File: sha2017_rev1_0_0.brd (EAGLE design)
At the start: 95 x 86 mm, 205 parts, among them IC1 CP210X_USB_UART, IC2 AP7215, IC3 ESP32WROOM32, IC4 TP4056, IC5 FXL6408, IC6 CPT112, M1 MOTOR10MM, Q1 MMBT2222A, Q2 MMBT2222A, Q3 MMBT2222A, Q4 MMBT2222A, Q5 SI1304 BDL, Q6 MMBT2222A, X2 2908-05WB-MG, X4 JST-PH3

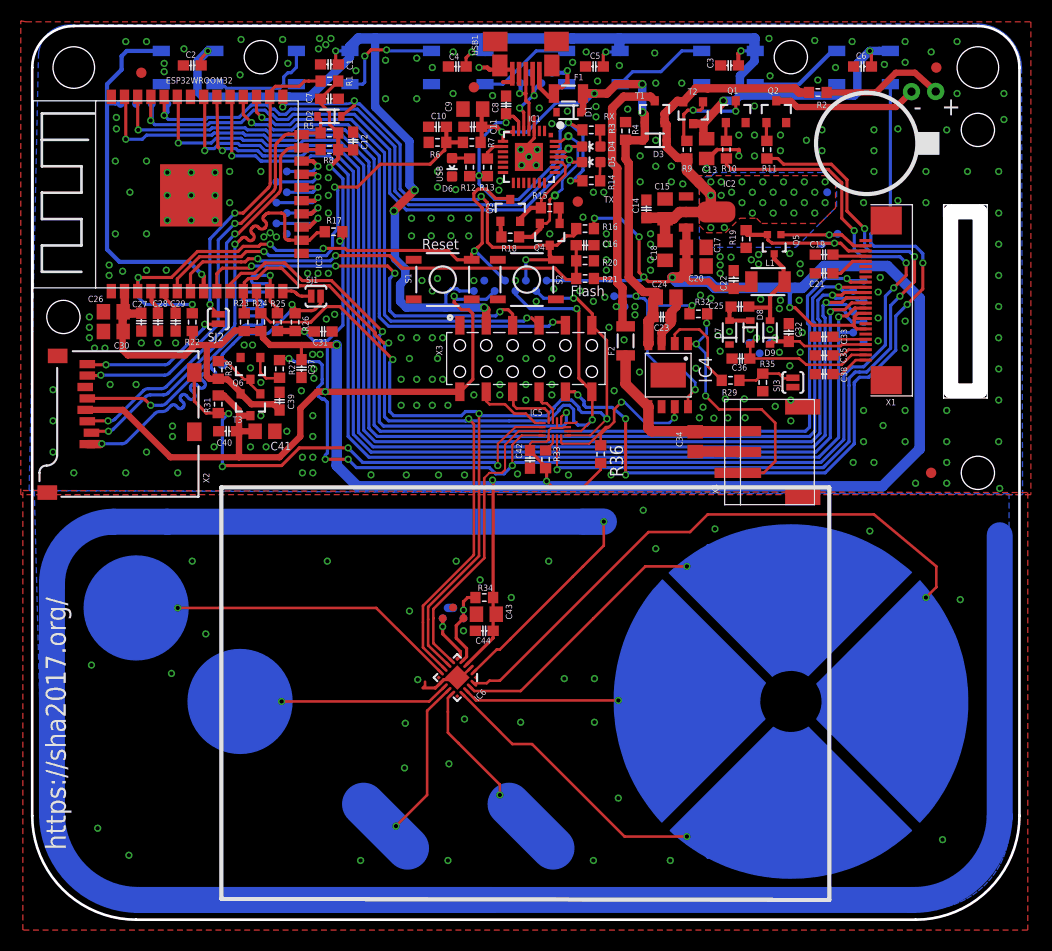
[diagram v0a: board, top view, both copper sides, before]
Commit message: Swap port expander and CPT112S for MPR121
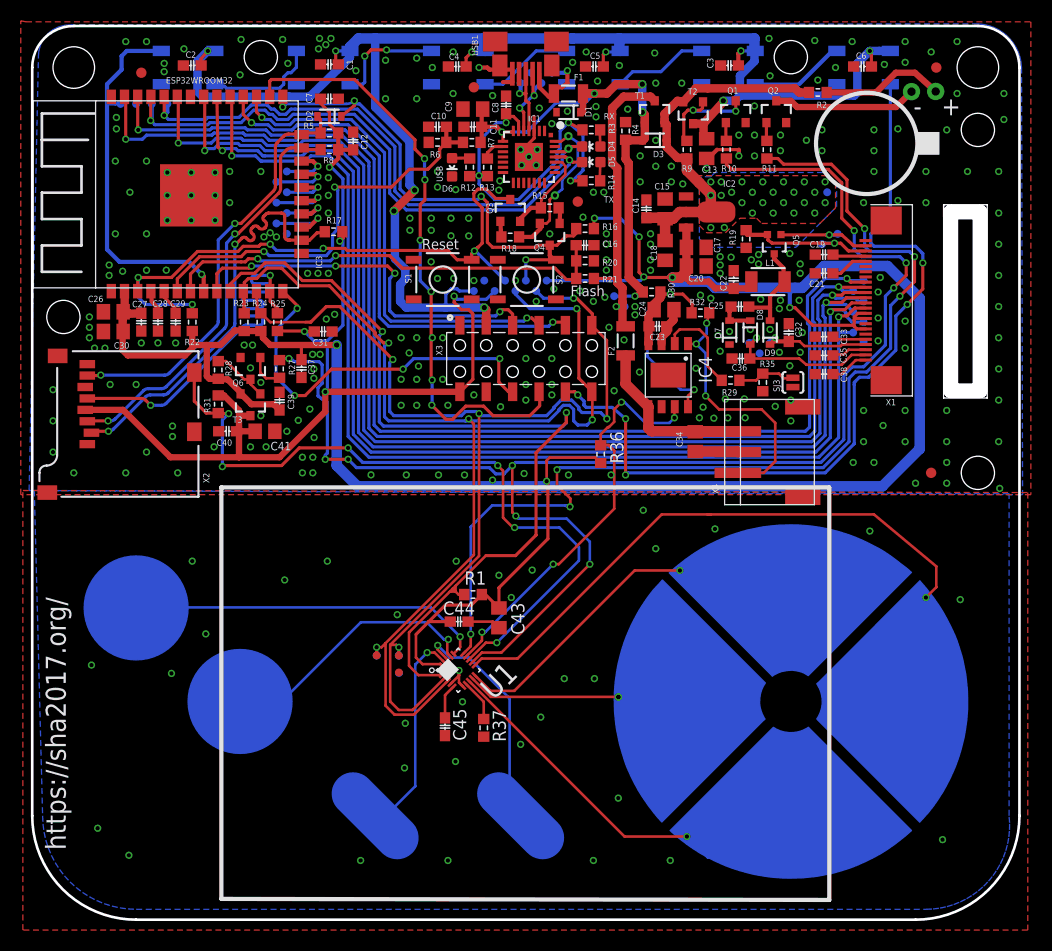
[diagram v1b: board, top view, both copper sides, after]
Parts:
- removed C42: 100n, sha2017_rev0_1_0_dev:C0603-DASHES
- removed IC5: FXL6408, badge:UMLP-16
- removed IC6: CPT112, badge:QFN20-3X3MM
- removed R26, R33: 10k, sha2017_rev0_1_0_dev:R0603-DASHES
- removed R34: 1k, sha2017_rev0_1_0_dev:R0603-DASHES
- removed SJ1, SJ2: JUMPER-PAD-2-NOYES_SILK, SparkFun-Passives:PAD-JUMPER-2-NO_YES_SILK
- removed TB100, TB101: TOUCHSELECT, badge:TOUCH_SELECT
- added C45: 100n, sha2017_rev0_1_0_dev:C0603-DASHES
- added R30: 150k, sha2017_rev0_1_0_dev:R0603-DASHES
- added R37: 75k 1%, sha2017_rev0_1_0_dev:R0603-DASHES
- added TOUCH_SELECT, TOUCH_START: TOUCHSELECT, badge:TOUCH_SELECT
- added U1: MPR121QR2, Freescale_By_element14_Batch_1:QFN40P300X300X60-20N
- R1: value 10k -> 100k; device 00ralf:R0603-DASHES -> sha2017_rev0_1_0_dev:R0603-DASHES
- R32: value 150k -> 10k
- moved R1 51.3 mm to (42.4, 30.3)
- moved U$11 13.9 mm to (40.7, 14.2)
- moved TP102 8.14 mm to (35.3, 22.7)
- moved TP1 8.14 mm to (35.3, 22.8)
- moved TP101 7.30 mm to (33.1, 24.4), turned to 180 degrees
- moved TP2 7.30 mm to (33.1, 24.4), turned to 180 degrees
- moved TP100 7.18 mm to (35.3, 24.4)
- moved TP3 7.18 mm to (35.3, 24.4)
- moved U$13 6.11 mm to (41.4, 20.0)
- moved $$U$9 4.07 mm to (41.1, 23.0)
- moved C44 2.57 mm to (41.1, 27.7), turned to 0 degrees
- moved U$10 2.13 mm to (47.0, 15.9)
- moved U$23 1.86 mm to (44.9, 32.1)
- moved U$6 1.80 mm to (48.1, 32.6)
- moved C43 1.26 mm to (44.9, 28.0), turned to 270 degrees
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- renumbered TB102 to TOUCH_SEL, TB103 to TOUCH_B, TB104 to TOUCH_A
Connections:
- removed net EXTIO-5: IC5.5, X3.11
- removed net N$55: IC6.19, TOUCH_SEL.UP
- removed net N$57: IC6.17, TOUCH_SEL.D
- removed net N$58: IC6.13, TOUCH_B.P$1
- removed net N$59: IC5.10, R33.2
- removed net N$61: IC6.5, R34.1, TP100.P$1, TP3.P$1
- removed net N$62: IC6.6, TP101.P$1, TP2.P$1
- removed net N$64: IC6.14, TB101.P$1
- removed net N$65: IC6.15, TB100.P$1
- removed net PROXIMITY: IC6.2
- removed net SD_DATA1: IC3.26, R1.1, SJ2.1
- removed net SD_DATA2: IC3.14, SJ1.1
- removed net SD_DATA2_OUT: R26.1, SJ1.2, X2.1
- removed net TOUCH_INT: IC5.7, IC6.7
- new net N$12: C23.2, C24.1, IC4.4, IC4.8, R30.2, R32.2
- new net N$20: C45.1, U1.5
- new net N$21: R37.2, U1.7
- new net N$24: TOUCH_B.P$1, U1.17
- new net N$44: TOUCH_SEL.D, U1.8
- new net N$46: TOUCH_SELECT.P$1, U1.18
- new net N$47: TOUCH_SEL.UP, U1.10
- net +3V3: now also R1.2, U1.20; no longer C42.1, IC5.15, IC5.2, IC5.9, IC6.4, R33.1, R34.2
- net +5V: now also R30.1; no longer C23.2, C24.1, IC4.4, IC4.8, R32.2
- net 3V3_SWITCHED: no longer R1.2, R26.2
- net CHRG_STAT: now also U1.14; no longer IC5.12
- net EXTIO-3: now also IC3.26; no longer IC5.3
- net EXTIO-4: now also IC3.14; no longer IC5.4
- net GND: now also C45.2, R37.1, U1.4, U1.6, X3.11; no longer C42.2, IC5.16, IC6.12, IC6.3
- net I2C_INT: now also R1.1, U1.1; no longer IC5.1
- net I2C_SCL: now also TP100.P$1, TP3.P$1, U1.2; no longer IC5.13, IC6.8
- net I2C_SDA: now also TP101.P$1, TP2.P$1, U1.3; no longer IC5.14, IC6.9
- net N$1: now also U1.16; no longer IC6.10
- net N$25: now also U1.11; no longer IC6.20
- net N$56: now also U1.9; no longer IC6.18
- net N$6: now also TOUCH_START.P$1, U1.19; no longer SJ2.2, X2.8
- net SD_CD: now also U1.13; no longer IC5.6
- net VIBRATOR: now also U1.15; no longer IC5.11
- net WS2812_POWER_EN: now also U1.12; no longer IC5.8
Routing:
- net PROXIMITY: track 258.4 -> 0.00 mm, vias 1 -> 0
- net EXTIO-3: track 3.57 -> 58.2 mm, vias 0 -> 6
- net N$55: track 39.8 -> 0.00 mm, vias 1 -> 0
- net N$57: track 39.6 -> 0.00 mm, vias 1 -> 0
- net N$44: track 0.00 -> 39.6 mm, vias 0 -> 1
- net N$47: track 0.00 -> 38.6 mm, vias 0 -> 1
- net I2C_INT: track 48.1 -> 85.2 mm
- net SD_DATA2_OUT: track 36.1 -> 0.00 mm, vias 2 -> 0
- net EXTIO-4: track 5.80 -> 37.4 mm, vias 0 -> 4
- net SD_DATA1: track 30.7 -> 0.00 mm, vias 2 -> 0
- net TOUCH_INT: track 29.2 -> 0.00 mm
- net +5V: track 82.7 -> 55.0 mm, vias 7 -> 5
- net N$24: track 0.00 -> 27.4 mm, vias 0 -> 1
- net N$12: track 0.00 -> 25.9 mm, vias 0 -> 2
- net WS2812_POWER_EN: track 116.3 -> 141.7 mm, vias 7 -> 9
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- removed copper zone on layer 1, net +5V

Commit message: Reverted power switches, re-routed touch controller
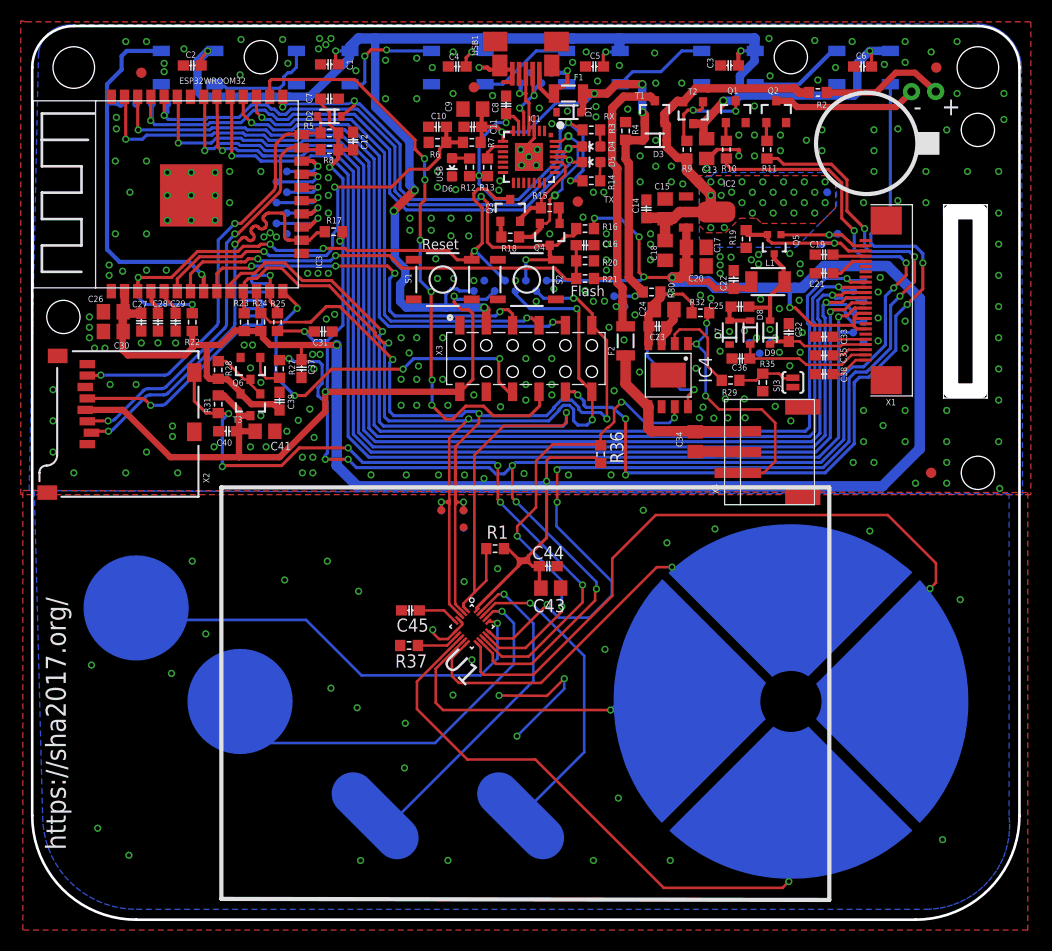
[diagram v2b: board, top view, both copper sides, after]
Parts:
- moved U$6 22.5 mm to (28.7, 21.3)
- moved $$U$8 16.3 mm to (38.5, 26.9)
- moved TP100 15.3 mm to (41.5, 38.4)
- moved TP102 15.3 mm to (41.5, 36.7)
- moved TP3 15.3 mm to (41.5, 38.4)
- moved TP1 15.3 mm to (41.5, 36.8)
- moved TP101 15.3 mm to (39.4, 38.4)
- moved TP2 15.3 mm to (39.4, 38.4)
- moved C45 11.7 mm to (36.4, 28.8), turned to 180 degrees
- moved U$11 10.8 mm to (31.3, 19.4)
- moved R37 10.7 mm to (36.3, 25.4), turned to 0 degrees
- moved $$U$1 10.3 mm to (55.1, 25.0)
- moved C44 10.1 mm to (49.7, 33.0)
- moved C43 5.75 mm to (49.9, 30.9), turned to 0 degrees
- moved R1 4.90 mm to (44.5, 34.7)
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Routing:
- net I2C_SDA: track 112.8 -> 94.3 mm
- net N$44: track 39.6 -> 52.7 mm
- net N$6: track 22.0 -> 34.9 mm
- net GND: track 26.7 -> 39.1 mm, vias 294 -> 288
- net I2C_SCL: track 104.7 -> 92.9 mm
- net N$24: track 27.4 -> 37.0 mm
- net N$46: track 23.2 -> 31.8 mm
- net N$1: track 35.9 -> 43.2 mm
- net N$56: track 18.4 -> 25.5 mm, vias 2 -> 1
- net I2C_INT: track 85.2 -> 78.3 mm
- net +3V3: track 247.2 -> 240.8 mm
- net CHRG_STAT: track 40.0 -> 45.6 mm
- net N$47: track 38.6 -> 44.2 mm
- net N$25: track 69.0 -> 72.1 mm
- net VIBRATOR: track 98.7 -> 100.5 mm
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
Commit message: Fix airwire
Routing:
- net GND: track 39.1 -> 49.8 mm
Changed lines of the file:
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@@
 <wire x1="51.2" y1="22.2" x2="51.2" y2="21.21575" width="0.254" layer="16"/>
 <wire x1="51.2" y1="21.21575" x2="46.65075" y2="16.6665" width="0.254" layer="16"/>
+<wire x1="42.307" y1="24.005" x2="41.4365" y2="24.005" width="0.254" layer="16"/>
+<wire x1="41.4365" y1="24.005" x2="38.5425" y2="26.899" width="0.254" layer="16"/>
+<wire x1="40.48875" y1="20.61775" x2="38.61775" y2="20.61775" width="0.254" layer="16"/>
+<wire x1="38.61775" y1="20.61775" x2="35.9" y2="17.9" width="0.254" layer="16"/>
 <wire x1="81.6" y1="60.8" x2="80.2" y2="60.85" width="0" layer="19" extent="1-1"/>
 <wire x1="80.2" y1="56.35" x2="81.4" y2="56.9" width="0" layer="19" extent="1-1"/>
-<wire x1="40.48875" y1="20.61775" x2="42.307" y2="24.005" width="0" layer="19" extent="1-1"/>
 </signal>
 <signal name="USB_DN_CON">

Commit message: MarkusBec rerouting and fixes
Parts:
- R30: value 150k -> 0R27; device sha2017_rev0_1_0_dev:R0603-DASHES -> rcl:R1206
- moved U$4 19.0 mm to (32.5, 14.9)
- moved $$U$9 17.0 mm to (50.0, 39.2)
- moved $$U$3 13.9 mm to (27.2, 17.4)
- moved U$2 12.0 mm to (50.5, 29.8)
- moved U$23 6.72 mm to (38.6, 30.2)
- moved U$10 6.51 mm to (40.1, 16.3)
- moved U$6 6.17 mm to (32.7, 26.0)
- moved C43 6.10 mm to (43.8, 31.0)
- moved C44 5.91 mm to (43.8, 32.7)
- moved U$5 5.00 mm to (46.6, 31.5)
- moved TP1 4.40 mm to (37.4, 38.4)
- moved U$11 3.05 mm to (30.1, 22.2)
- moved U$13 2.31 mm to (47.1, 21.3)
- moved $$U$7 1.88 mm to (50.4, 23.9)
- moved U$12 1.50 mm to (36.8, 19.1)
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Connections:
- removed net N$56: TOUCH_SEL.R, U1.9
- new net N$48: TOUCH_SEL.R, U1.13
- net CHRG_STAT: now also U1.17; no longer U1.14
- net N$1: now also TOUCH_B.P$1, U1.9; no longer TOUCH_A.P$1, U1.16
- net N$24: now also TOUCH_START.P$1, U1.10; no longer TOUCH_B.P$1, U1.17
- net N$25: now also TOUCH_SELECT.P$1; no longer TOUCH_SEL.L
- net N$44: now also U1.12; no longer U1.8
- net N$46: now also TOUCH_SEL.L, U1.15; no longer TOUCH_SELECT.P$1, U1.18
- net N$47: now also U1.14; no longer U1.10
- net N$6: now also TOUCH_A.P$1, U1.8; no longer TOUCH_START.P$1, U1.19
- net SD_CD: now also U1.19; no longer U1.13
- net VIBRATOR: now also U1.16; no longer U1.15
- net WS2812_POWER_EN: now also U1.18; no longer U1.12
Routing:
- net N$25: track 72.1 -> 19.2 mm
- net N$46: track 31.8 -> 63.6 mm
- net N$56: track 25.5 -> 0.00 mm, vias 1 -> 0
- net N$48: track 0.00 -> 19.2 mm, vias 0 -> 1
- net N$1: track 43.2 -> 25.7 mm
- net +3V3: track 240.8 -> 225.2 mm
- net N$24: track 37.0 -> 21.8 mm
- net WS2812_POWER_EN: track 142.5 -> 130.3 mm, vias 9 -> 7
- net SD_CD: track 69.0 -> 58.6 mm, vias 6 -> 4
- net N$44: track 52.7 -> 44.3 mm
- net N$47: track 44.2 -> 36.3 mm
- net GND: track 49.8 -> 41.9 mm, vias 288 -> 298
- net VIBRATOR: track 100.5 -> 93.2 mm, vias 6 -> 4
- net CHRG_STAT: track 45.6 -> 39.9 mm, vias 4 -> 2
- net N$12: track 25.9 -> 30.5 mm
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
